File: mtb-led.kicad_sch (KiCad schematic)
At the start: 58 parts, among them J7 AVR-ISP-6, J9 DEBUG, SW1 SW_Push, U1 ATmega328PB-A, U2 78M05, U3 TLC5940PWP, U4 TLC5940PWP, U5 MAX487E, Y1 14.7456 MHz

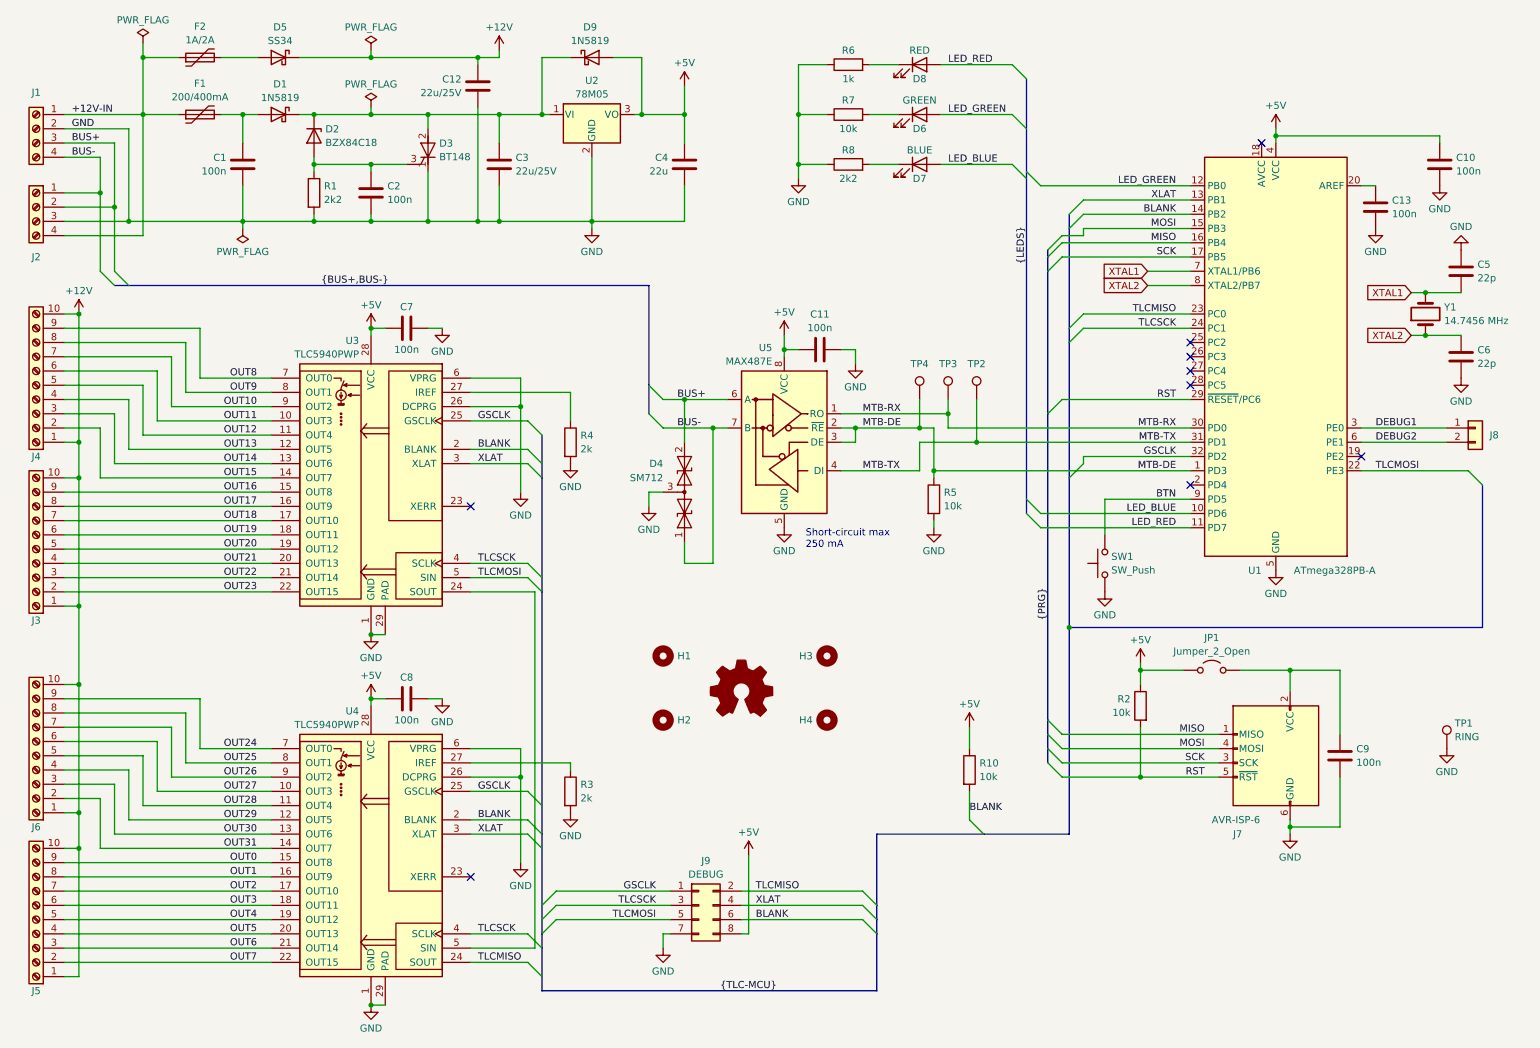
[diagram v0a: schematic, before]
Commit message: Sch: add I2C interface to ambient light sensor.
E.g. BH1750.
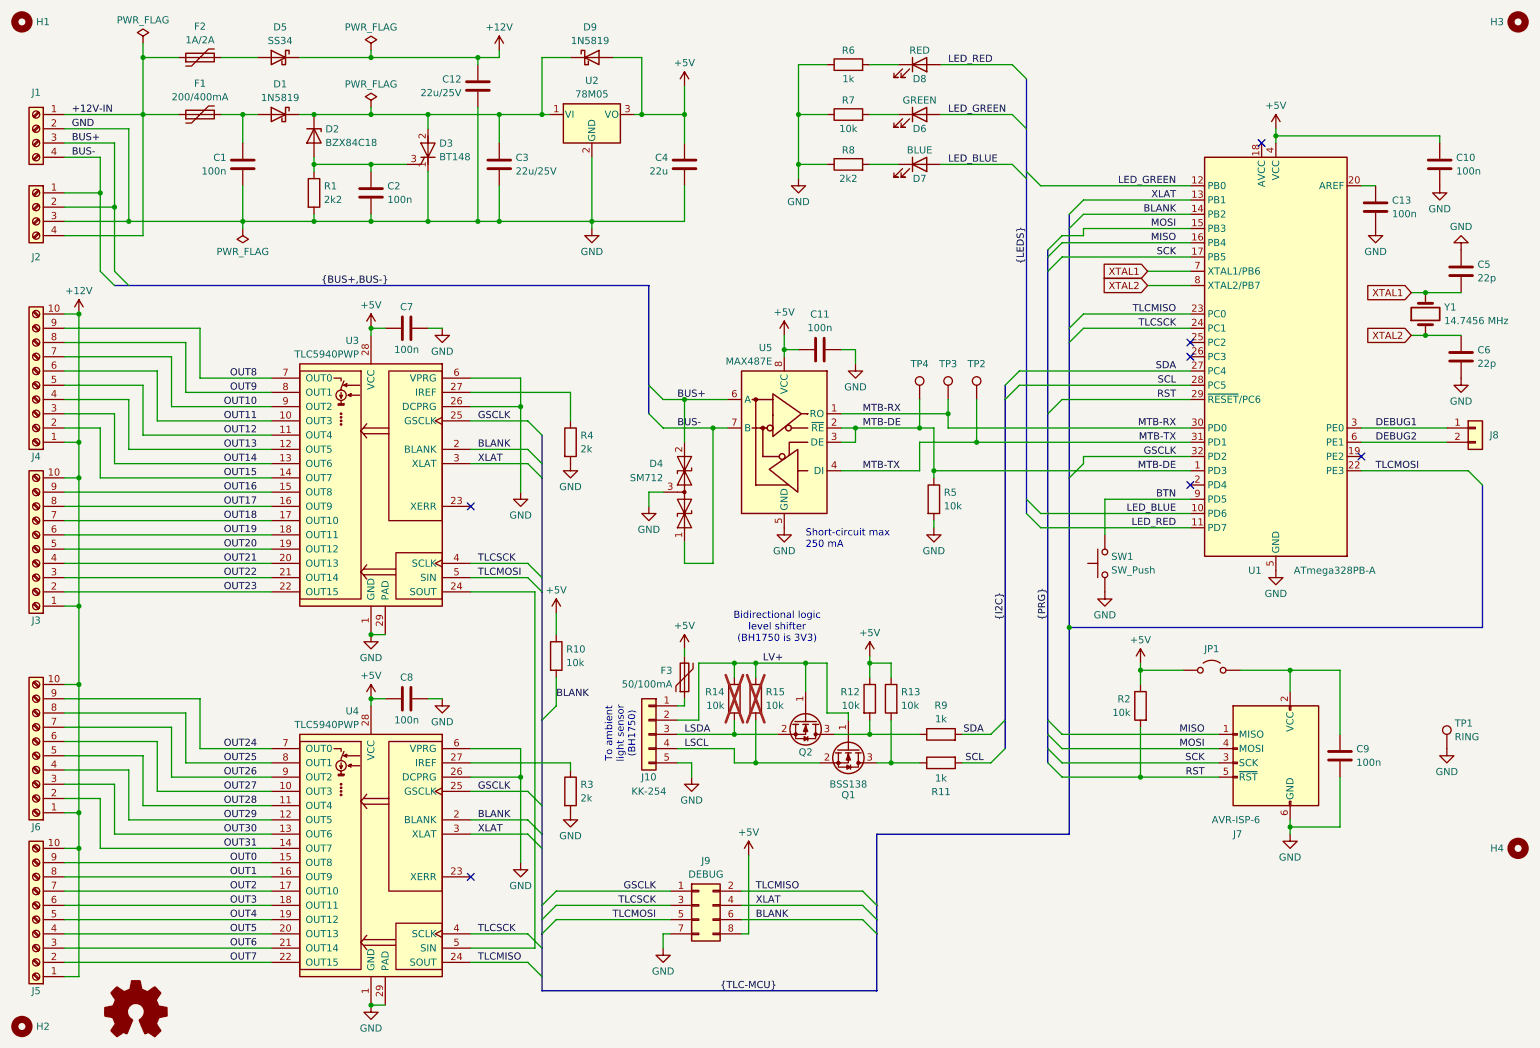
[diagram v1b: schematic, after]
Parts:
- added F3: 50/100mA, Fuse:Fuse_1206_3216Metric, symbol Device:Polyfuse
- added J10: KK-254, Connector_Molex:Molex_KK-254_AE-6410-05A_1x05_P2.54mm_Vertical, symbol Connector_Generic:Conn_01x05
- added Q1, Q2: BSS138, Package_TO_SOT_SMD:SOT-23, symbol Transistor_FET:BSS138
- added R11, R9: 1k, Resistor_SMD:R_0805_2012Metric, symbol Device:R
- added R12, R13, R14, R15: 10k, Resistor_SMD:R_0805_2012Metric, symbol Device:R
- JP1: value Jumper_2_Open -> ~
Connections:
- net +5V: now also F3.2, R12.1, R13.1
- net GND: now also J10.5 (Pin_5)
- net SDA: now reaches U1.27 (PC4)
- net SDA: now also R9.2
- net SCL: now reaches U1.28 (PC5)
- net SCL: now also R11.2
- new net: Q2.3 (D), R12.2, R9.1
- new net: Q1.3 (D), R11.1, R13.2
- new net: F3.1, J10.1 (Pin_1)
- new net LSCL: J10.4 (Pin_4), Q1.2 (S), R15.2
- new net LSDA: J10.3 (Pin_3), Q2.2 (S), R14.2
- new net LV+: J10.2 (Pin_2), Q1.1 (G), Q2.1 (G), R14.1, R15.1
- no-connect marks 9 -> 7
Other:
- note added: "Bidirectional logic level shifter (BH1750 is 3V3)"
- note added: "To ambient light sensor (BH1750)"
- moved on the sheet: H1, H2, H3, H4, R10

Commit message: PCB: wire light sensor connection.
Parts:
- F3: LCSC (none) -> C2830235
- J10: JLCPCB_IGNORE (none) -> true
- Q1, Q2: value BSS138 -> AO3400/BSS138; LCSC (none) -> C20917
- R11, R9: LCSC (none) -> C17513
- R12, R13: LCSC (none) -> C17414
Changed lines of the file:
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@@
 			)
 		)
-		(property "Value" "BSS138"
+		(property "Value" "AO3400/BSS138"
 			(at 149.86 152.4 90)
 			(effects
@@
 			)
 		)
+		(property "LCSC" "C20917"
+			(at 154.94 139.7 90)
+			(effects
+				(font
+					(size 1.27 1.27)
+				)
+				(hide yes)
+			)
+		)
 		(pin "2"
 		)
@@
 			)
 		)
-		(property "Value" "BSS138"
+		(property "Value" "AO3400/BSS138"
 			(at 162.56 151.13 90)
 			(effects
@@
 			)
 		)
+		(property "LCSC" "C20917"
+			(at 162.56 144.78 90)
+			(effects
+				(font
+					(size 1.27 1.27)
+				)
+				(hide yes)
+			)
+		)
 		(pin "2"
 		)
@@
 			)
 		)
+		(property "LCSC" "C17513"
+			(at 179.07 142.24 90)
+			(effects
+				(font
+					(size 1.27 1.27)
+				)
+				(hide yes)
+			)
+		)
 		(pin "1"
 		)
@@
 			)
 		)
+		(property "LCSC" "C17414"
+			(at 170.18 135.89 0)
+			(effects
+				(font
+					(size 1.27 1.27)
+				)
+				(hide yes)
+			)
+		)
 		(pin "2"
 		)
@@
 			)
 		)
+		(property "JLCPCB_IGNORE" "true"
+			(at 127 142.24 0)
+			(effects
+				(font
+					(size 1.27 1.27)
+				)
+				(hide yes)
+			)
+		)
 		(pin "4"
 		)
@@
 			)
 		)
+		(property "LCSC" "C2830235"
+			(at 133.35 132.08 0)
+			(effects
+				(font
+					(size 1.27 1.27)
+				)
+				(hide yes)
+			)
+		)
 		(pin "2"
 		)
@@
 			)
 		)
+		(property "LCSC" "C17414"
+			(at 166.37 135.89 0)
+			(effects
+				(font
+					(size 1.27 1.27)
+				)
+				(hide yes)
+			)
+		)
 		(pin "2"
 		)
@@
 			(effects
 				(font
+					(size 1.27 1.27)
+				)
+				(hide yes)
+			)
+		)
+		(property "LCSC" "C17513"
+			(at 179.07 147.32 90)
+			(effects
+				(font

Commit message: Enhance thermal conductivity from TLC5940.
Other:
- note added: "All LEDs on: 1.5-3 W of heat / TLC! (depends on number of LEDs in circuits)"
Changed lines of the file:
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@@
+		)
+	)
+	(text "All LEDs on: 1.5-3 W of heat / TLC!\n(depends on number of LEDs in circuits)"
+		(exclude_from_sim no)
+		(at 50.8 128.27 0)
+		(effects
+			(font
+				(size 1.27 1.27)
+				(thickness 0.254)
+				(bold yes)
+				(color 194 0 0 1)
+			)
 		)
 	)

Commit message: Better thermal connection of TLC5940.
We need to dissipate as max heat as possible.
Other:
- note added: "0.64 A max"
- note added: "All LEDs on: 1.5-3 W of heat / TLC! → 3-6 W total! (depends on number of LEDs in circuits)"
- note removed: "All LEDs on: 1.5-3 W of heat / TLC! (depends on number of LEDs in circuits)"
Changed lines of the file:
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@@
 		)
 	)
-	(text "All LEDs on: 1.5-3 W of heat / TLC!\n(depends on number of LEDs in circuits)"
+	(text "All LEDs on: 1.5-3 W of heat / TLC!\n→ 3-6 W total!\n(depends on number of LEDs in circuits)"
 		(exclude_from_sim no)
 		(at 50.8 128.27 0)
@@
 		)
 	)
+	(text "0.64 A max"
+		(exclude_from_sim no)
+		(at 83.82 20.32 0)
+		(effects
+			(font
+				(size 1.27 1.27)
+			)
+			(justify left)
+		)
+	)
